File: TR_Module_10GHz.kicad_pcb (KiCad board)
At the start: 4 copper layers, 35 x 70 mm, 45 parts, among them J1 Card Edge 40-pin, Q1 MOSFET, U1 LM5156 SEPIC, U10 QPC0045 RX, U11 SN74HC595, U12 SN74LVTH573, U13 TMP117 QPM1002, U14 TMP117 SEPIC, U15 TMP117 PS, U16 TMP117 PCB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

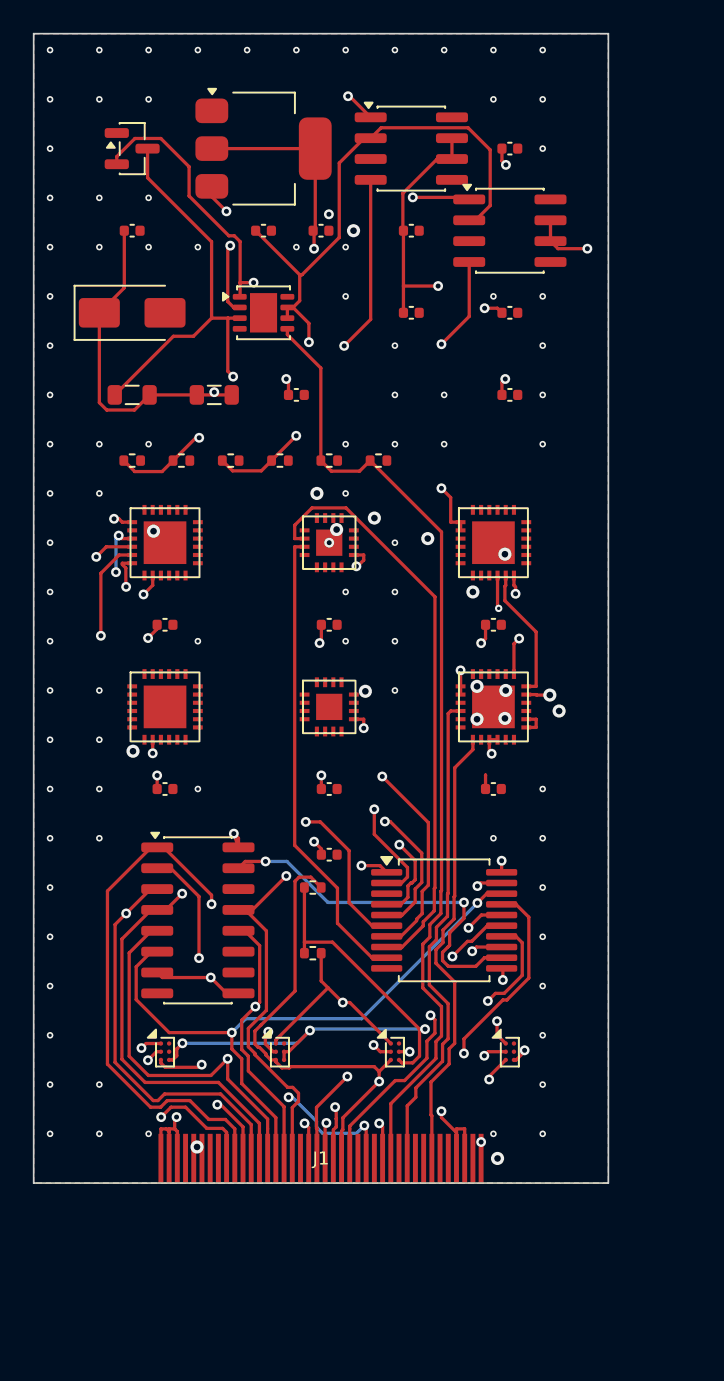
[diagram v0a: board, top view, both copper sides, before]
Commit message: update: autorouted PCB (22/36 nets, 1789 segments)
Co-authored-by: Qwen-Coder <qwen-coder@alibabacloud.com>
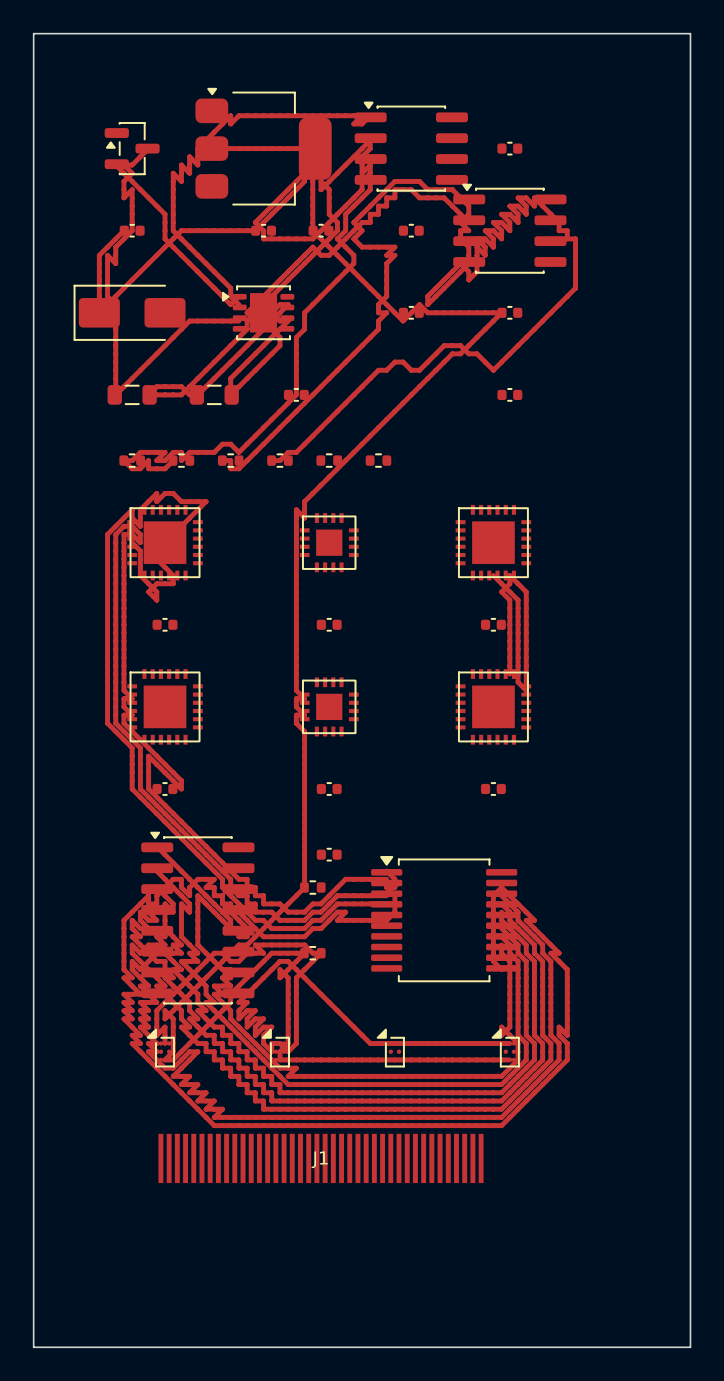
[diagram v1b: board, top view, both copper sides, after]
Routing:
- net BOOT_5V: track 64.5 -> 0.00 mm, vias 2 -> 0
- net EN_BOOST: track 71.9 -> 12.1 mm, vias 2 -> 0
- net FB_SEPIC: track 58.9 -> 0.00 mm
- net SR_QA: track 53.6 -> 0.00 mm, vias 3 -> 0
- net I2C_SDA: track 51.6 -> 0.00 mm, vias 3 -> 0
- net SW_SEPIC: track 78.9 -> 28.7 mm, vias 3 -> 0
- net BOOT_10V: track 76.3 -> 28.2 mm, vias 3 -> 0
- net SR_RCLK: track 32.6 -> 80.0 mm, vias 2 -> 0
- net +10V: track 45.8 -> 0.00 mm, vias 2 -> 0
- net VG: track 45.9 -> 6.41 mm, vias 3 -> 0
- net CTRL_TX_PS1: track 0.00 -> 37.1 mm
- net CTRL_TX_PS3: track 36.5 -> 0.00 mm, vias 2 -> 0
- net CTRL_TX_ATT0: track 35.7 -> 0.00 mm
- net CTRL_TX_PS5: track 35.2 -> 0.00 mm, vias 2 -> 0
- net CTRL_TX_PS4: track 32.8 -> 0.00 mm, vias 2 -> 0
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- removed copper zone on In2.Cu, net +5V
- removed copper zone on B.Cu, net GND
- removed copper zone on F.Cu, net GND
- removed copper zone on In1.Cu, net GND
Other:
- board size 35 x 70 mm -> 40 x 80 mm

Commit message: Revert "update: autorouted PCB (22/36 nets, 1789 segments)"
This reverts commit aaf4b5bc0dab927e93ae8dcb000f6a615e5b2f24.
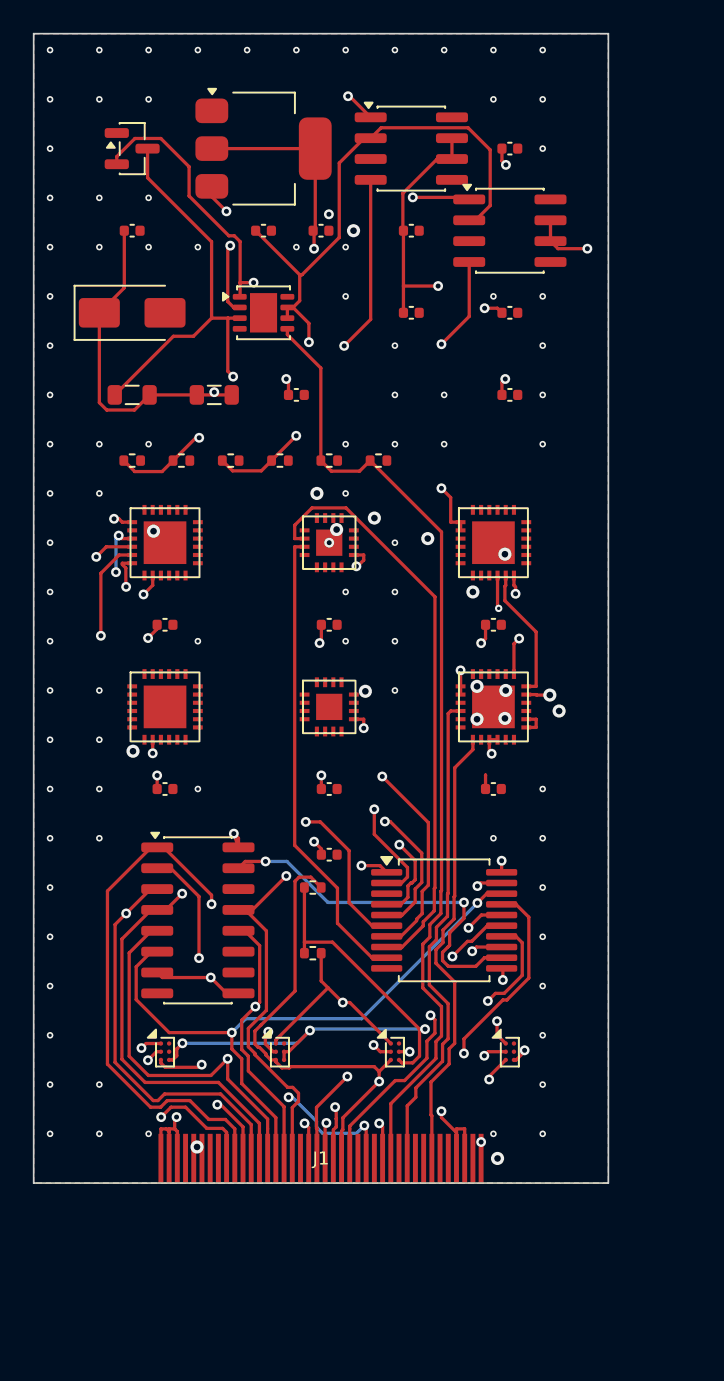
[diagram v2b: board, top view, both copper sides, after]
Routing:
- net BOOT_5V: track 0.00 -> 64.5 mm, vias 0 -> 2
- net EN_BOOST: track 12.1 -> 71.9 mm, vias 0 -> 2
- net FB_SEPIC: track 0.00 -> 58.9 mm
- net SR_QA: track 0.00 -> 53.6 mm, vias 0 -> 3
- net I2C_SDA: track 0.00 -> 51.6 mm, vias 0 -> 3
- net SW_SEPIC: track 28.7 -> 78.9 mm, vias 0 -> 3
- net BOOT_10V: track 28.2 -> 76.3 mm, vias 0 -> 3
- net SR_RCLK: track 80.0 -> 32.6 mm, vias 0 -> 2
- net +10V: track 0.00 -> 45.8 mm, vias 0 -> 2
- net VG: track 6.41 -> 45.9 mm, vias 0 -> 3
- net CTRL_TX_PS1: track 37.1 -> 0.00 mm
- net CTRL_TX_PS3: track 0.00 -> 36.5 mm, vias 0 -> 2
- net CTRL_TX_ATT0: track 0.00 -> 35.7 mm
- net CTRL_TX_PS5: track 0.00 -> 35.2 mm, vias 0 -> 2
- net CTRL_TX_PS4: track 0.00 -> 32.8 mm, vias 0 -> 2
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- added copper zone on In2.Cu, net +5V
- added copper zone on B.Cu, net GND
- added copper zone on F.Cu, net GND
- added copper zone on In1.Cu, net GND
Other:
- board size 40 x 80 mm -> 35 x 70 mm
